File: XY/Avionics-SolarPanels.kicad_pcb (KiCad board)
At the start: 4 copper layers, 82 x 100 mm, 202 parts, among them J1 200528-0100, J2 200528-0100, Q1 IRLML2803, Q17 NX3008NBKS, Q18 MBT2222ADW1T1, Q19 NX3008NBKS, Q2 SIRA99DP-T1-GE3, Q20 MBT2222ADW1T1, Q21 NX3008NBKS, Q22 MBT2222ADW1T1, Q23 NX3008NBKS, Q24 MBT2222ADW1T1, Q25 NX3008NBKS, Q26 MBT2222ADW1T1, Q7 NX3008NBKS, Q8 MBT2222ADW1T1, U1 LTC4412xS6, U10 LTC3130, U11 LTC3130, U12 LTC3130, U13 ADM1176-1ARMZ-R7, U2 DRV8235RTER, U3 CSD25402Q3A, U4 LTC4412xS6, U5 OPT4003DNPRQ1, U6 USBLC6-2P6, U7 CSD25402Q3A, U8 LTC4412xS6, U9 CSD25402Q3A

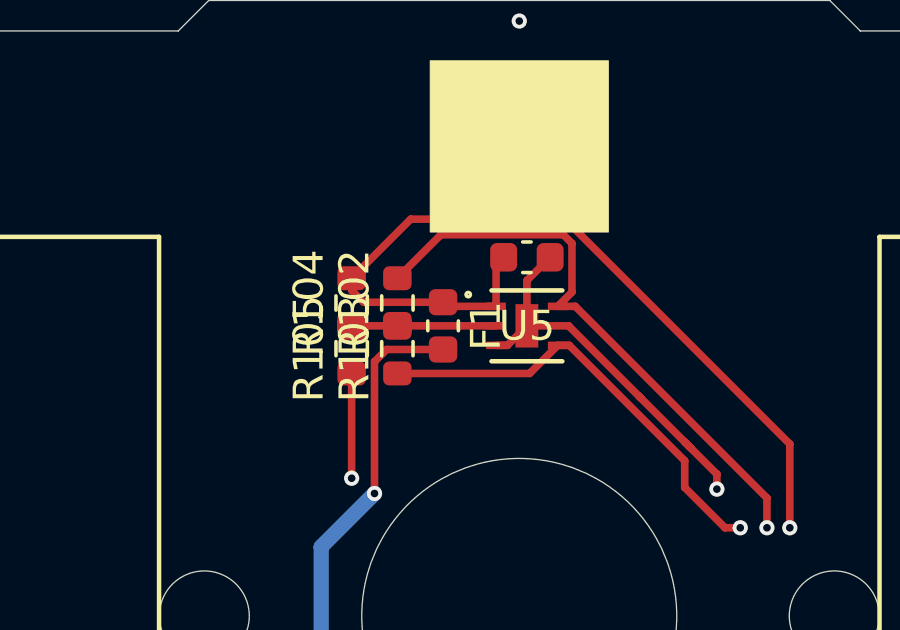
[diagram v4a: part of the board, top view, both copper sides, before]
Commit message: Updated silkscreen
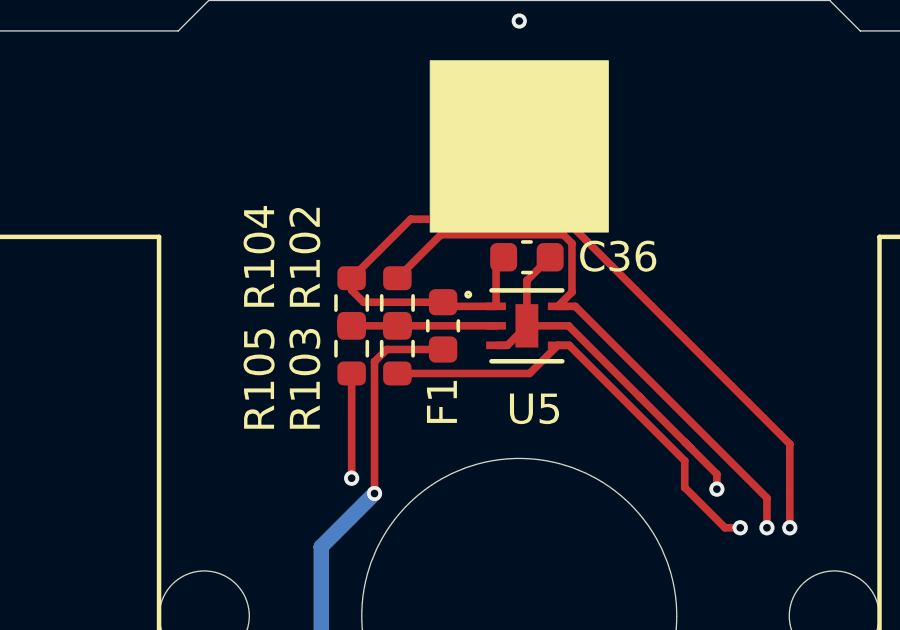
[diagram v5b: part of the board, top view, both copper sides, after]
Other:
- board text added: "VSLR1"
- board text added: "VSLR2"
- board text removed: "DVSOLAR1"
- board text removed: "DVSOLAR2"

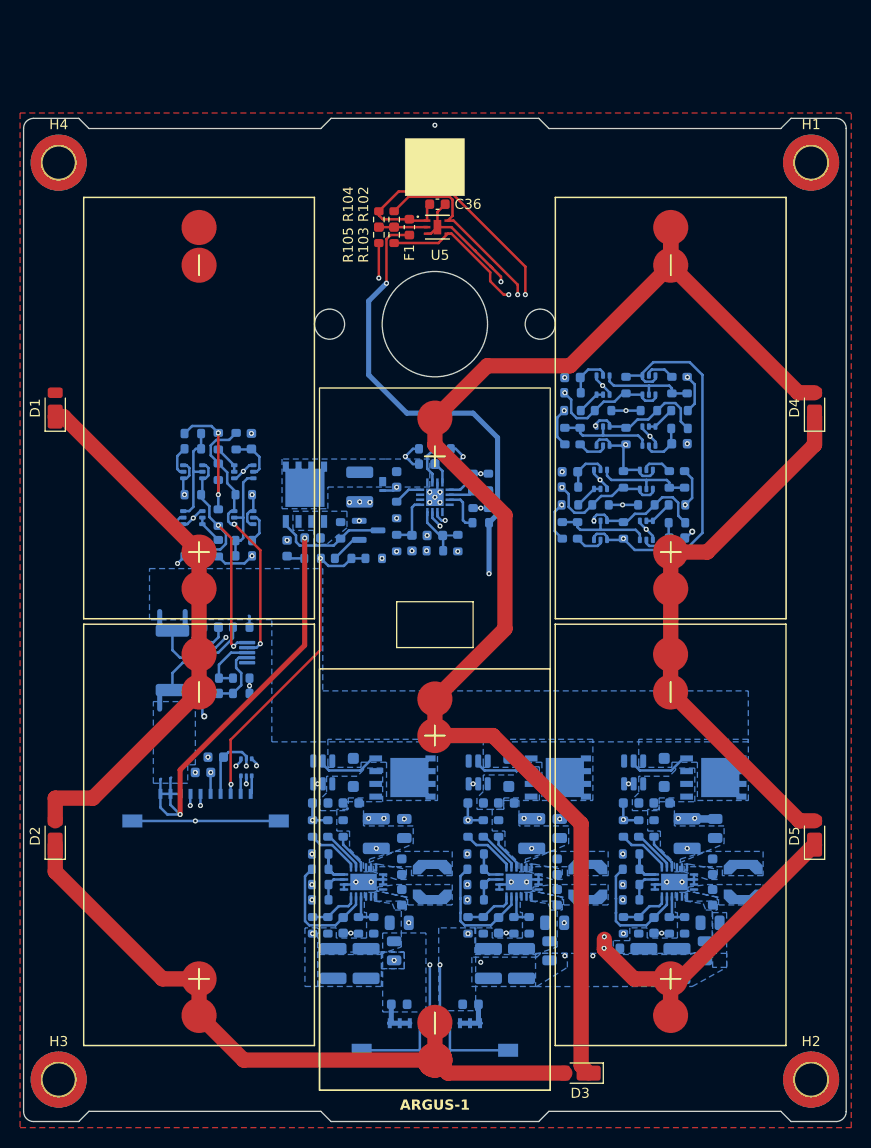
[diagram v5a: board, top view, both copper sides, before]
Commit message: Added USBc cutout?
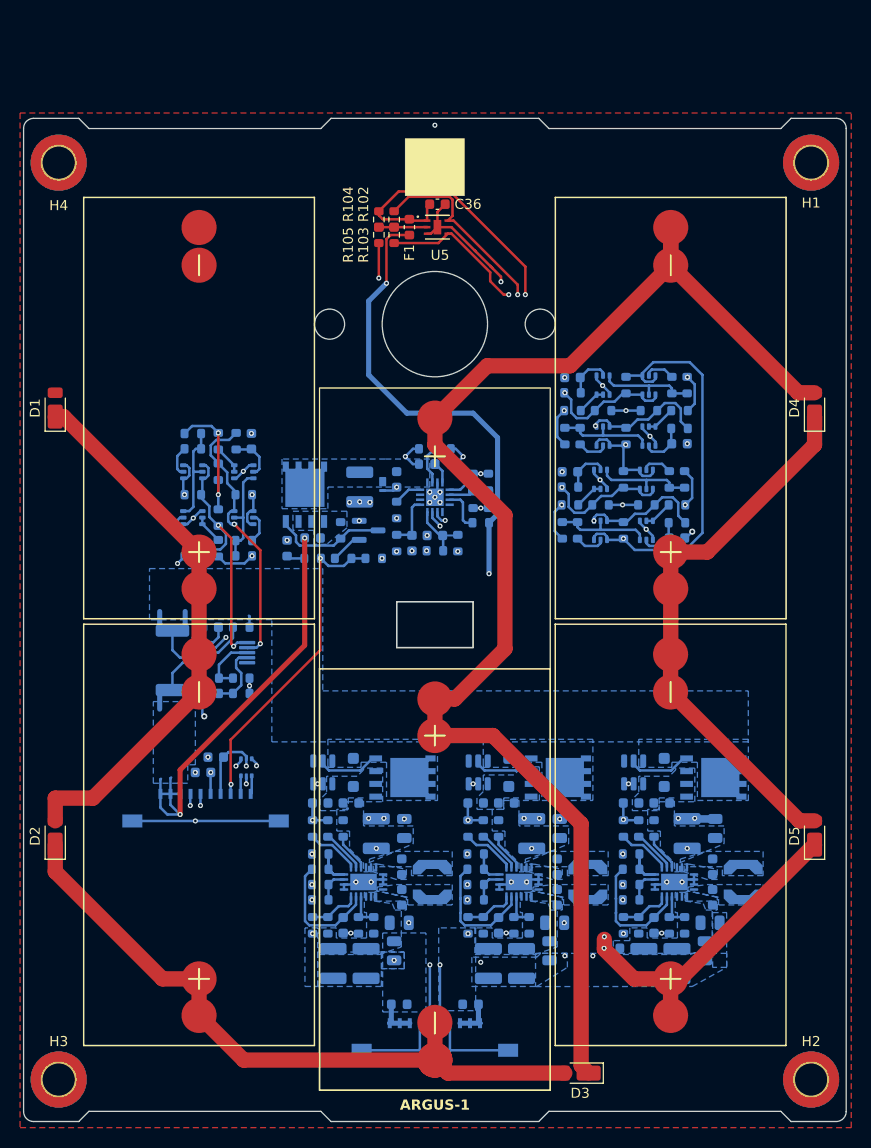
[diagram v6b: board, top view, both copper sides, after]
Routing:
- net Net-(D3-K): track 134.9 -> 136.0 mm
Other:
- outline, holes or cut-outs redrawn
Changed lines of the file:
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@@
 		(tags "mounting hole 3.2mm m3 din965")
 		(property "Reference" "H1"
-			(at 0 -3.8 0)
+			(at 0 4.016799 0)
 			(layer "F.SilkS")
 			(effects
@@
 		(tags "mounting hole 3.2mm m3 din965")
 		(property "Reference" "H4"
-			(at 0 -3.8 0)
+			(at 0 4.2672 0)
 			(layer "F.SilkS")
 			(effects
@@
 		(tags "resistor")
 		(property "Reference" "R38"
-			(at -5.08 0.254 90)
+			(at 3.556 -0.254 90)
 			(layer "B.SilkS")
 			(effects
@@
 		(tags "resistor")
 		(property "Reference" "R39"
-			(at 0 -4.572 0)
+			(at 0 -1.778 0)
 			(layer "B.SilkS")
 			(effects
@@
 		)
 	)
+	(gr_line
+		(start 163.322 111.76)
+		(end 163.576 111.506)
+		(stroke
+			(width 0.1)
+			(type default)
+		)
+		(layer "B.SilkS")
+	)
 	(gr_arc
 		(start 191.100001 126.41619)
@@
 		(layer "B.SilkS")
 	)
+	(gr_line
+		(start 165.862 111.76)
+		(end 163.322 111.76)
+		(stroke
+			(width 0.1)
+			(type default)
+		)
+		(layer "B.SilkS")
+	)
+	(gr_line
+		(start 122.428 107.696)
+		(end 122.682 107.442)
+		(stroke
+			(width 0.1)
+			(type default)
+		)
+		(layer "B.SilkS")
+	)
+	(gr_line
+		(start 177.546 112.014)
+		(end 177.8 112.268)
+		(stroke
+			(width 0.1)
+			(type default)
+		)
+		(layer "B.SilkS")
+	)
 	(gr_arc
 		(start 125.7 141.42198)
@@
 	)
 	(gr_line
+		(start 177.546 112.014)
+		(end 177.8 111.76)
+		(stroke
+			(width 0.1)
+			(type default)
+		)
+		(layer "B.SilkS")
+	)
+	(gr_line
 		(start 134.7597 128.143)
 		(end 134.7597 128.778)
@@
 		(layer "B.SilkS")
 	)
+	(gr_line
+		(start 148.336 111.506)
+		(end 148.082 111.76)
+		(stroke
+			(width 0.1)
+			(type default)
+		)
+		(layer "B.SilkS")
+	)
+	(gr_line
+		(start 122.428 105.156)
+		(end 122.428 107.696)
+		(stroke
+			(width 0.1)
+			(type default)
+		)
+		(layer "B.SilkS")
+	)
+	(gr_line
+		(start 148.082 111.76)
+		(end 148.336 112.014)
+		(stroke
+			(width 0.1)
+			(type default)
+		)
+		(layer "B.SilkS")
+	)
+	(gr_line
+		(start 163.576 111.506)
+		(end 163.322 111.76)
+		(stroke
+			(width 0.1)
+			(type default)
+		)
+		(layer "B.SilkS")
+	)
 	(gr_arc
 		(start 130.467382 56.4162)
@@
 	)
 	(gr_line
+		(start 177.8 111.76)
+		(end 177.546 112.014)
+		(stroke
+			(width 0.1)
+			(type default)
+		)
+		(layer "B.SilkS")
+	)
+	(gr_line
 		(start 172.7 148.3897)
 		(end 172.6946 151.2824)
@@
 	)
 	(gr_line
+		(start 180.086 112.014)
+		(end 177.546 112.014)
+		(stroke
+			(width 0.1)
+			(type default)
+		)
+		(layer "B.SilkS")
+	)
+	(gr_line
 		(start 124.3203 128.778)
 		(end 124.3203 128.1684)
@@
 		(layer "B.SilkS")
 	)
+	(gr_line
+		(start 122.428 107.696)
+		(end 122.174 107.442)
+		(stroke
+			(width 0.1)
+			(type default)
+		)
+		(layer "B.SilkS")
+	)
+	(gr_line
+		(start 163.322 111.76)
+		(end 163.576 112.014)
+		(stroke
+			(width 0.1)
+			(type default)
+		)
+		(layer "B.SilkS")
+	)
+	(gr_line
+		(start 122.174 107.442)
+		(end 122.428 107.696)
+		(stroke
+			(width 0.1)
+			(type default)
+		)
+		(layer "B.SilkS")
+	)
+	(gr_line
+		(start 148.082 111.76)
+		(end 148.336 111.506)
+		(stroke
+			(width 0.1)
+			(type default)
+		)
+		(layer "B.SilkS")
+	)
+	(gr_line
+		(start 150.622 111.76)
+		(end 148.082 111.76)
+		(stroke
+			(width 0.1)
+			(type default)
+		)
+		(layer "B.SilkS")
+	)
 	(gr_arc
 		(start 180.1096 63.4238)
@@
 	)
 	(gr_line
+		(start 156.21 100.584)
+		(end 148.59 100.584)
+		(stroke
+			(width 0.05)
+			(type default)
+		)
+		(layer "Edge.Cuts")
+	)
+	(gr_line
 		(start 141.0334 151.38408)
 		(end 117.91605 151.38408)
@@
 	)
 	(gr_line
+		(start 148.59 100.584)
+		(end 148.59 105.156)
+		(stroke
+			(width 0.05)
+			(type default)
+		)
+		(layer "Edge.Cuts")
+	)
+	(gr_line
+		(start 148.59 105.156)
+		(end 156.21 105.156)
+		(stroke
+			(width 0.05)
+			(type default)
+		)
+		(layer "Edge.Cuts")
+	)
+	(gr_line
 		(start 186.88405 151.38388)
 		(end 187.90015 152.39998)
@@
 	)
 	(gr_line
+		(start 156.21 105.156)
+		(end 156.21 100.584)
+		(stroke
+			(width 0.05)
+			(type default)
+		)
+		(layer "Edge.Cuts")
+	)
+	(gr_line
 		(start 141.0334 151.38408)
 		(end 142.0495 152.40018)
@@
 	)
 	(segment
-		(start 152.4 110.2786)
-		(end 159.385 103.2936)
-		(width 1.524)
-		(layer "F.Cu")
-		(net 46)
-	)
-	(segment
 		(start 175.9077 67.04)
 		(end 188.6227 79.755)
@@
 	)
 	(segment
-		(start 159.385 91.945776)
-		(end 152.4 84.960776)
+		(start 154.3894 110.2786)
+		(end 159.385 105.283)
 		(width 1.524)
 		(layer "F.Cu")
@@
 	)
 	(segment
-		(start 152.4 84.960776)
-		(end 152.4 82.2786)
+		(start 152.4 110.2786)
+		(end 154.3894 110.2786)
 		(width 1.524)
 		(layer "F.Cu")
@@
 	)
 	(segment
-		(start 159.385 103.2936)
+		(start 159.385 105.283)
 		(end 159.385 91.945776)
 		(width 1.524)
@@
 	)
 	(segment
+		(start 152.4 84.960776)
+		(end 152.4 82.2786)
+		(width 1.524)
+		(layer "F.Cu")
+		(net 46)
+	)
+	(segment
 		(start 188.6227 79.755)
 		(end 190.246 79.755)
 		(width 1.524)
 		(layer "F.Cu")
+		(net 46)
+	)
+	(segment
+		(start 159.385 91.945776)
+		(end 152.4 84.960776)
+		(width 1.524)
+		(layer "F.Cu")

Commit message: Updated 3d models, footprints
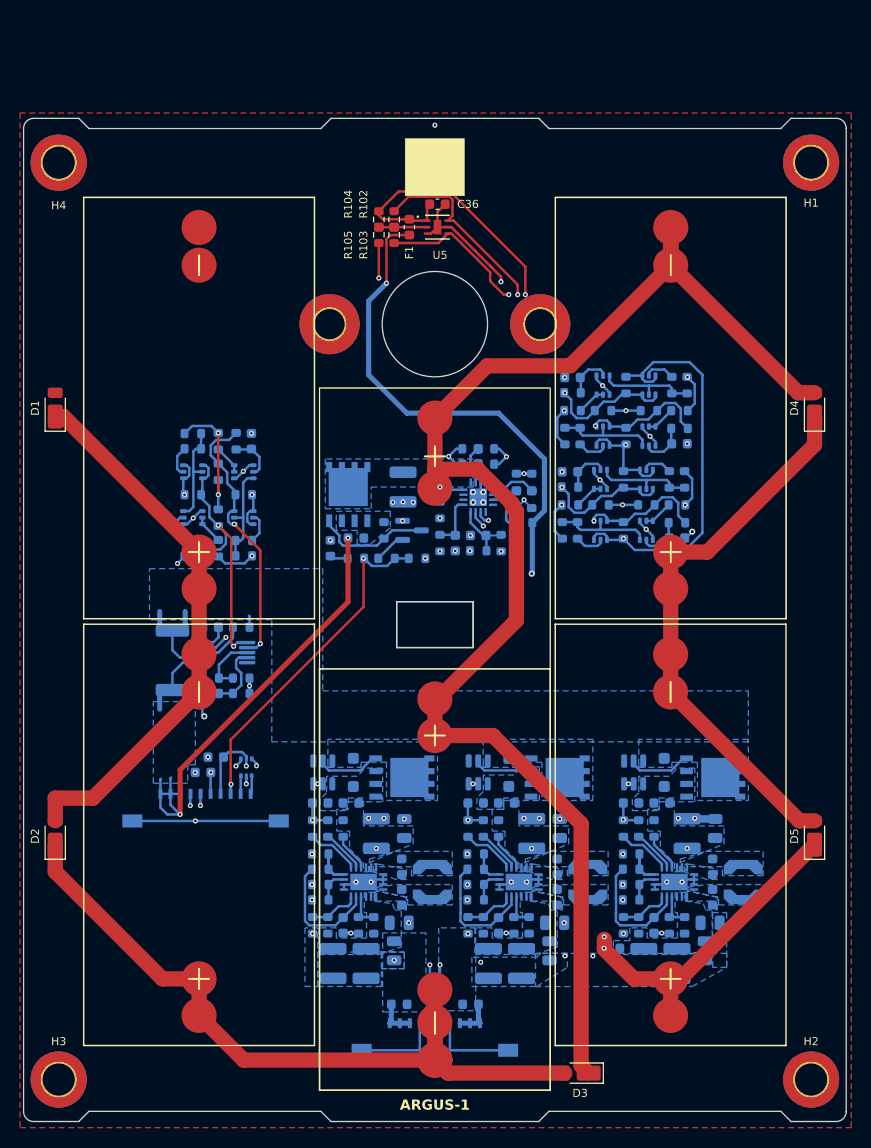
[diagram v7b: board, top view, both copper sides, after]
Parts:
- removed U3, U7, U9: CSD25402Q3A, Package_SO:PowerPAK_SO-8_Single
- added Q3: SiRA99DP, Argus-Miscellaneous:PowerPAK SO-8, B.Cu at (180.8, 118.1)
- added Q4: SiRA99DP, Argus-Miscellaneous:PowerPAK SO-8, B.Cu at (165.3, 118.1)
- added Q5: SiRA99DP, Argus-Miscellaneous:PowerPAK SO-8, B.Cu at (149.9, 118.1)
- H5, H6: footprint MountingHole:MountingHole_3mm -> MountingHole:MountingHole_3mm_Pad_TopBottom
- J1, J2: footprint Connector_FFC-FPC:Molex_200528-0100_1x10-1MP_P1.00mm_Horizontal -> Argus-Connectors:Molex_200528-0100_1x10-1MP_P1.00mm_Horizontal
- L1, L2, L3: footprint Inductor_SMD:L_Coilcraft_LPS4018 -> Argus-Passives:L_Coilcraft_LPS4018
- Q2: value SIRA99DP-T1-GE3 -> SiRA99DP; footprint Package_SO:PowerPAK_SO-8_Single -> Argus-Miscellaneous:PowerPAK SO-8
- moved Q2 4.38 mm to (143.8, 89.2), turned to -90 degrees
- moved F2 4.32 mm to (144.5, 94.2)
- moved Q1 4.32 mm to (150.1, 93.5)
- moved R36 4.32 mm to (144.5, 96.3)
- moved R37 4.32 mm to (150.6, 96.3)
- moved R39 4.32 mm to (147.6, 96.3)
- moved C22 4.32 mm to (154.4, 94.7)
- moved C26 4.32 mm to (149.2, 89.2)
- moved C27 4.32 mm to (152.9, 88.4)
- moved C28 4.32 mm to (156.7, 94.0)
- moved D10 4.32 mm to (151.5, 88.9)
- moved D9 4.32 mm to (142.0, 95.2)
- moved R28 4.32 mm to (156.0, 85.3)
- moved R29 4.32 mm to (157.5, 85.3)
- moved R30 4.32 mm to (157.5, 86.9)
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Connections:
- F2 pad 1: Net-(F2-Pad1) -> Net-(Q2-S)
- Q2 pad 1: Net-(F2-Pad1) -> Net-(Q1-D)
- Q2 pad 2: Net-(F2-Pad1) -> /Coil Driver/VM
- Q2 pad 3: Net-(F2-Pad1) -> Net-(Q2-S)
- R38 pad 2: Net-(F2-Pad1) -> Net-(Q2-S)
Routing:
- net PERI_3V3: track 91.7 -> 99.6 mm
- net Net-(D2-K): track 67.7 -> 74.7 mm
- net /Coil Driver/SCL_M: track 29.1 -> 24.6 mm
- net /Coil Driver/SDA_M: track 29.3 -> 24.9 mm
- net Net-(D3-K): track 136.0 -> 140.4 mm
- net VBATT: track 56.7 -> 58.5 mm
- net COIL_DRIVER_EN: track 32.3 -> 34.1 mm
- net MAIN_3V3: track 38.4 -> 39.1 mm
- net GND: vias 79 -> 78
- added copper zone on B.Cu, net Net-(Q2-S)
- removed copper zone on B.Cu, net Net-(F2-Pad1)
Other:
- board text added: "COIL EN"
